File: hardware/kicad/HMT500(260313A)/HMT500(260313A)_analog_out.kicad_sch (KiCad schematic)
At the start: 27 parts, among them U10 TPS26611, U12 OPA197IDBVR, U13 OPA197IDBVR, U7 DAC8760IPWP, U8 DAC8760IPWP, U9 TPS26611

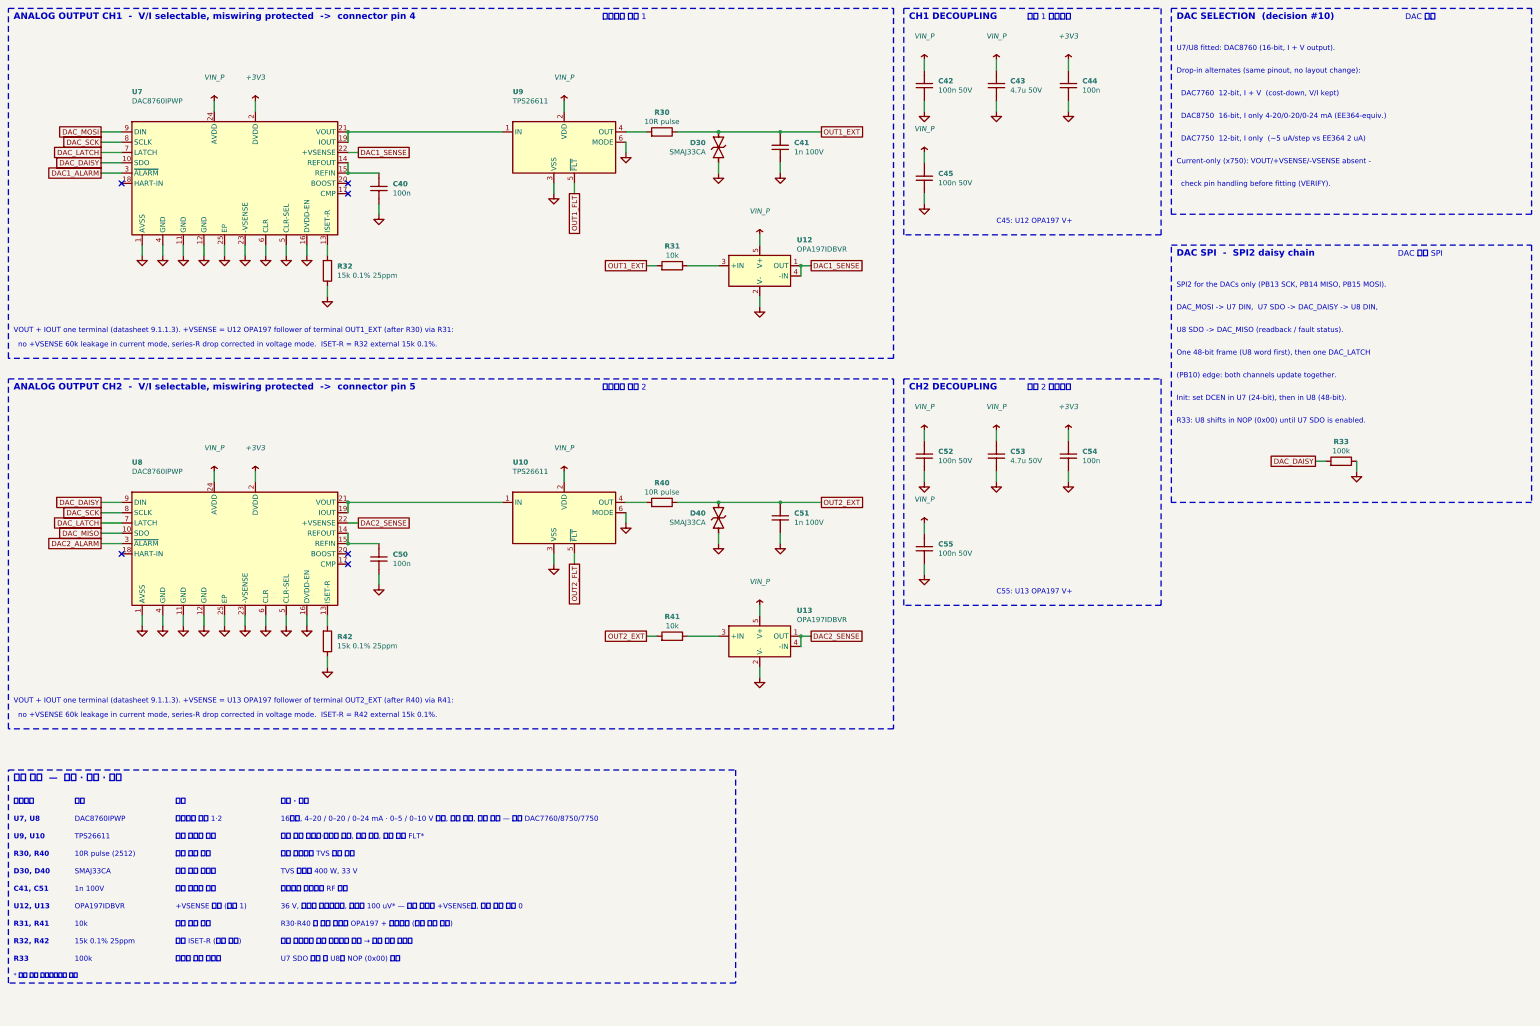
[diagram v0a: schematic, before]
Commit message: Schematic v0.8: apply datasheet review A-O (HMT500(260313A))
- Real pinouts from manufacturer datasheets: LMR36006BRNXR (RNX-12),
  TPS26611DDFR (SOT-23-8), PCAP04 (QFN24); TPS2660 PowerPAD = RTN
- TPS2660: RTN isolated from GND (R22, R7 removed); R5/R6/C4/MODE on
  EF_RTN; R6 80.6k (149 mA); R5 41.2k -> OVP 29 V, supply 12-28 V so
  TPS26611 +Vs stays <= 30 V
- DAC SPI: per-DAC SCLK gating (74LVC2G32, SPI2 mode 3, LATCH1/2 on
  PB10/PB11) - daisy chain was removed in DAC8760 rev D
- DAC AVDD 10R series, ALARM wired-OR with 10k pull-up (PB6)
- Output TVS -> TVS3301 (stacked-pin two-terminal symbol)
- PCAP04 on dedicated SPI3 (PB3/4/5), VDD18 4.7uF, VDD33 10uF
- Buck per datasheet: L 15uH, COUT 2x22uF, CFF 20pF
- Shared VIN_P bulk (C53, C26 removed); PWR_FLT PB7; SGOOD -> PC6/PC7
- Parts list, circuit-design, decision log #26, review doc updated;
  netlist 74/74, 0 errors; tests pass

Co-Authored-By: Claude Opus 5.5 <noreply@anthropic.com>
Claude-Session: https://claude.ai/code/session_01JA2o8uJsqp9Vzsg4b665ev
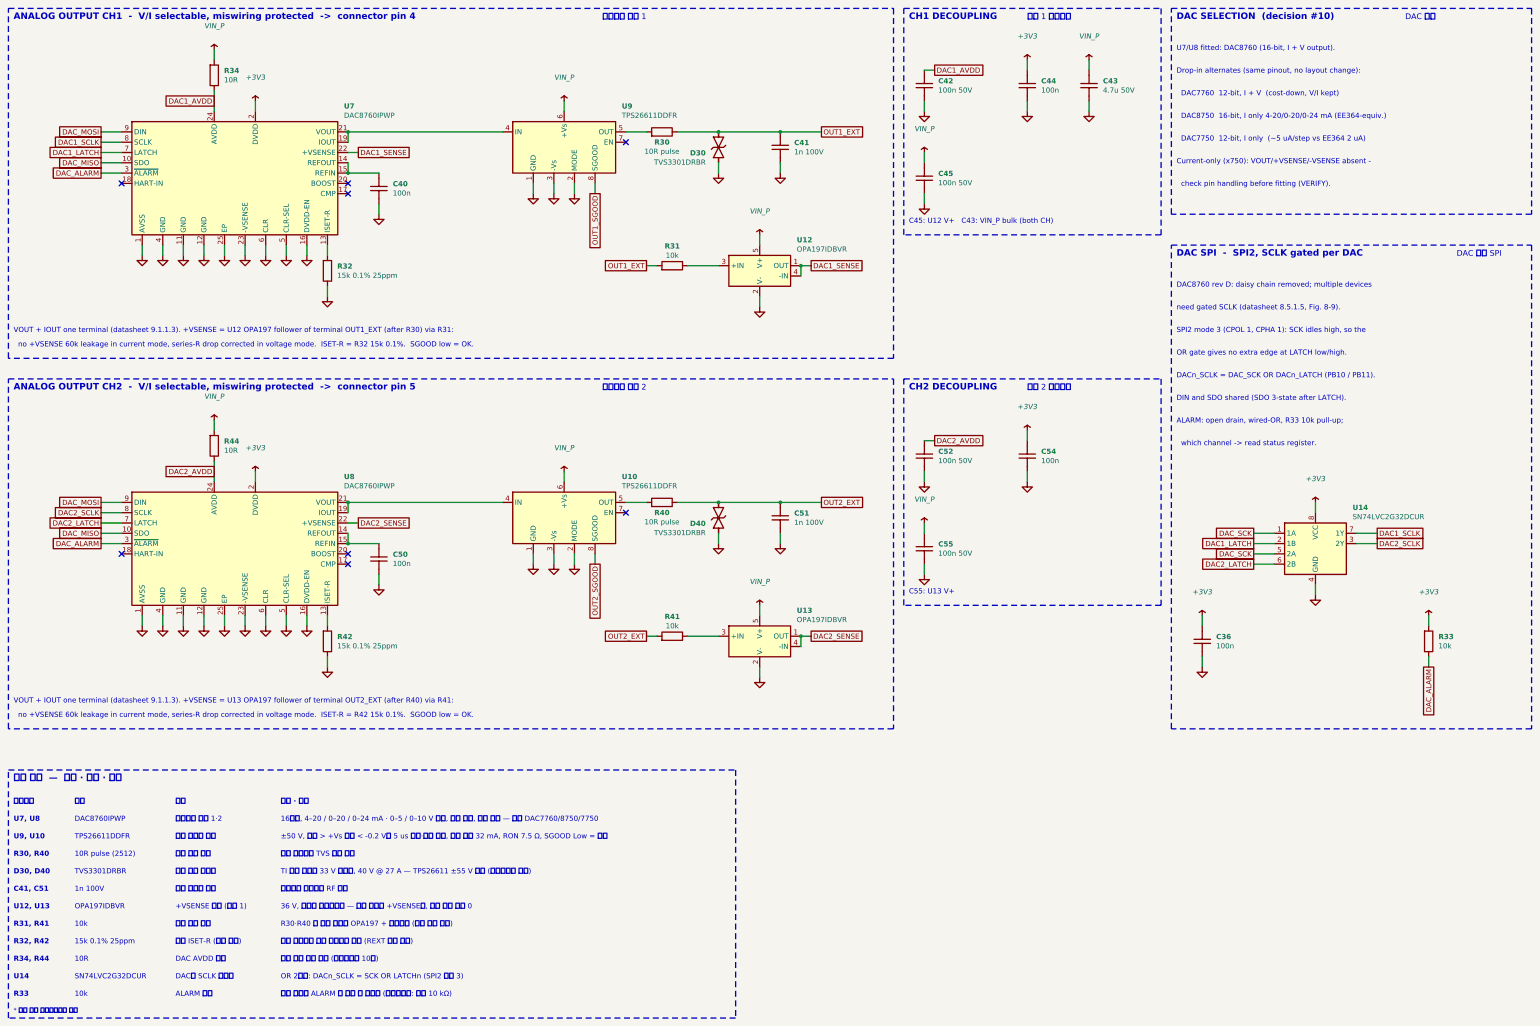
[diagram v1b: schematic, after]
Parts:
- removed C53: 4.7u 50V, Capacitor_SMD:C_1210_3225Metric, symbol HMT500_260313A:C
- added C36: 100n, Capacitor_SMD:C_0603_1608Metric, symbol HMT500_260313A:C
- added R34, R44: 10R, Resistor_SMD:R_0603_1608Metric, symbol HMT500_260313A:R
- added U14: SN74LVC2G32DCUR, Package_SO:VSSOP-8_2.3x2mm_P0.5mm, symbol HMT500_260313A:74LVC2G32
- D30, D40: value SMAJ33CA -> TVS3301DRBR; footprint Diode_SMD:D_SMA -> Package_DFN_QFN:Texas_DRB0008A; symbol HMT500_260313A:TVS_BI -> HMT500_260313A:TVS3301
- R33: value 100k -> 10k
- U10, U9: value TPS26611 -> TPS26611DDFR; footprint TBD:TPS26611 -> Package_TO_SOT_SMD:Texas_DDF0008A_SOT-8_1.6x2.9mm_P0.65mm; VERIFY YES - pin numbers are placeholders -> (none)
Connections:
- net DAC2_ALARM is gone; now on net DAC_ALARM: U8.3 (~{ALARM})
- net OUT1_FLT is gone; now on an unnamed net: U9.5 (OUT)
- net OUT2_FLT is gone; now on an unnamed net: U10.5 (OUT)
- net +3V3: now also R33.1, C36.1, U14.8 (VCC)
- net DAC_MISO: now also U7.10 (SDO)
- net DAC_MOSI: now also U8.9 (DIN)
- net DAC_SCK: now also U14.1 (1A), U14.5 (2A); no longer U7.8 (SCLK), U8.8 (SCLK)
- net GND: now also D30.5, D30.6, D30.7, D30.8, D40.5, D40.6, D40.7, D40.8, U10.1 (GND), U10.2 (MODE), U9.1 (GND), U9.2 (MODE), C36.2, U14.4 (GND); no longer D30.2, D40.2, R33.2, U10.6 (MODE), U9.6 (MODE)
- net OUT1_EXT: now also D30.2, D30.3, D30.4
- net OUT2_EXT: now also D40.2, D40.3, D40.4
- net VIN_P: now also U10.6 (+Vs), U9.6 (+Vs), R34.1, R44.1; no longer C42.1, C52.1, U10.2 (VDD), U7.24 (AVDD), U8.24 (AVDD), U9.2 (VDD)
- net at R30.1: no longer U9.4 (OUT)
- net at U8.19 (IOUT), U8.21 (VOUT): now also U10.4 (IN); no longer U10.1 (IN)
- net at R40.1: no longer U10.4 (OUT)
- net at U7.19 (IOUT), U7.21 (VOUT): now also U9.4 (IN); no longer U9.1 (IN)
- net DAC1_ALARM renamed DAC_ALARM
- net DAC_ALARM: now also R33.2
- removed net DAC_DAISY: R33.1, U7.10 (SDO), U8.9 (DIN)
- net DAC_LATCH renamed DAC1_LATCH
- net DAC1_LATCH: now also U14.2 (1B); no longer U8.7 (LATCH)
- new net DAC1_AVDD: C42.1, R34.2, U7.24 (AVDD)
- new net DAC1_SCLK: U14.7 (1Y), U7.8 (SCLK)
- new net DAC2_AVDD: C52.1, R44.2, U8.24 (AVDD)
- new net DAC2_LATCH: U14.6 (2B), U8.7 (LATCH)
- new net DAC2_SCLK: U14.3 (2Y), U8.8 (SCLK)
- new net OUT1_SGOOD: U9.8 (SGOOD)
- new net OUT2_SGOOD: U10.8 (SGOOD)
- no-connect marks 6 -> 8
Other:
- note added: "10R"
- note added: "36 V, 입출력 레일투레일 — 단자 전압을 +VSENSE로, 전류 모드 누설 0"
- note added: "ALARM 풀업"
- note added: "ALARM: open drain, wired-OR, R33 10k pull-up;"
- note added: "C45: U12 V+ C43: VIN_P bulk (both CH)"
- note added: "C55: U13 V+"
- note added: "DAC AVDD 직렬"
- note added: "DAC SPI - SPI2, SCLK gated per DAC"
- note added: "DAC8760 rev D: daisy chain removed; multiple devices"
- note added: "DACn_SCLK = DAC_SCK OR DACn_LATCH (PB10 / PB11)."
- note added: "DAC별 SCLK 게이트"
- note added: "DIN and SDO shared (SDO 3-state after LATCH)."
- note added: "OR 2회로: DACn_SCLK = SCK OR LATCHn (SPI2 모드 3)"
- note added: "OR gate gives no extra edge at LATCH low/high."
- note added: "R34, R44"
- note added: "SN74LVC2G32DCUR"
- note added: "SPI2 mode 3 (CPOL 1, CPHA 1): SCK idles high, so the"
- note added: "TI 평탄 클램프 33 V 양방향, 40 V @ 27 A — TPS26611 ±55 V 보호 (데이터시트 권장)"
- note added: "TPS26611DDFR"
- note added: "TVS3301DRBR"
- note added: "U14"
- note added: "need gated SCLK (datasheet 8.5.1.5, Fig. 8-9)."
- note added: "no +VSENSE 60k leakage in current mode, series-R drop corrected in voltage mode. ISET-R = R32 15k 0.1%. SGOOD low = OK."
- note added: "no +VSENSE 60k leakage in current mode, series-R drop corrected in voltage mode. ISET-R = R42 15k 0.1%. SGOOD low = OK."
- note added: "which channel -> read status register."
- note added: "±50 V, 단자 > +Vs 또는 < -0.2 V면 5 us 차단·자동 복귀, 전류 제한 32 mA, RON 7.5 Ω, SGOOD Low = 정상"
- note added: "내부 저항보다 온도 드리프트 작음 (REXT 비트 설정)"
- note added: "오픈 드레인 ALARM 두 개를 한 선으로 (데이터시트: 외부 10 kΩ)"
- note added: "전원 상승 속도 제한 (데이터시트 10장)"
- note removed: "(PB10) edge: both channels update together."
- note removed: "100k"
- note removed: "36 V, 입출력 레일투레일, 오프셋 100 uV* — 단자 전압을 +VSENSE로, 전류 모드 누설 0"
- note removed: "C45: U12 OPA197 V+"
- note removed: "C55: U13 OPA197 V+"
- note removed: "DAC SPI - SPI2 daisy chain"
- note removed: "DAC_MOSI -> U7 DIN, U7 SDO -> DAC_DAISY -> U8 DIN,"
- note removed: "Init: set DCEN in U7 (24-bit), then in U8 (48-bit)."
- note removed: "One 48-bit frame (U8 word first), then one DAC_LATCH"
- note removed: "R33: U8 shifts in NOP (0x00) until U7 SDO is enabled."
- note removed: "SMAJ33CA"
- note removed: "SPI2 for the DACs only (PB13 SCK, PB14 MISO, PB15 MOSI)."
- note removed: "TPS26611"
- note removed: "TVS 양방향 400 W, 33 V"
- note removed: "U7 SDO 켜기 전 U8에 NOP (0x00) 입력"
- note removed: "U8 SDO -> DAC_MISO (readback / fault status)."
- note removed: "no +VSENSE 60k leakage in current mode, series-R drop corrected in voltage mode. ISET-R = R32 external 15k 0.1%."
- note removed: "no +VSENSE 60k leakage in current mode, series-R drop corrected in voltage mode. ISET-R = R42 external 15k 0.1%."
- note removed: "내부 저항보다 온도 드리프트 작음 → 전류 출력 정확도"
- note removed: "데이지 체인 풀다운"
- note removed: "출력 단자 과전압·역전압 차단, 전류 제한, 고장 출력 FLT*"
- moved on the sheet: C43, C44, C54, R33

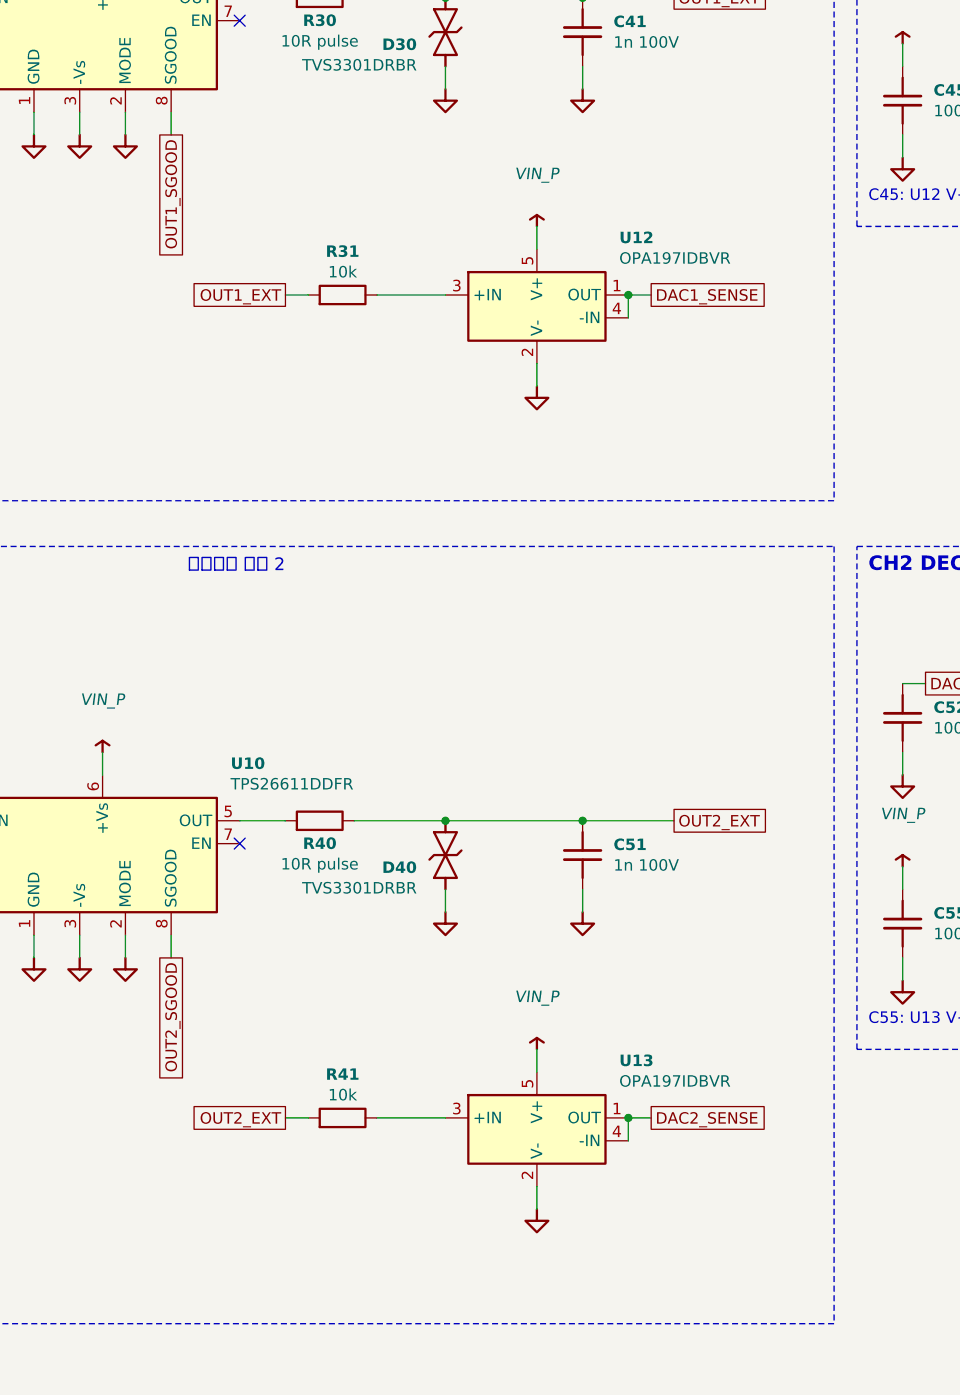
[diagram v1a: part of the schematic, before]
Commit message: Schematic: mirror OPA197 +VSENSE buffers (terminal on right, +VSENSE on left)
Co-Authored-By: Claude Opus 5.5 <noreply@anthropic.com>
Claude-Session: https://claude.ai/code/session_01JA2o8uJsqp9Vzsg4b665ev
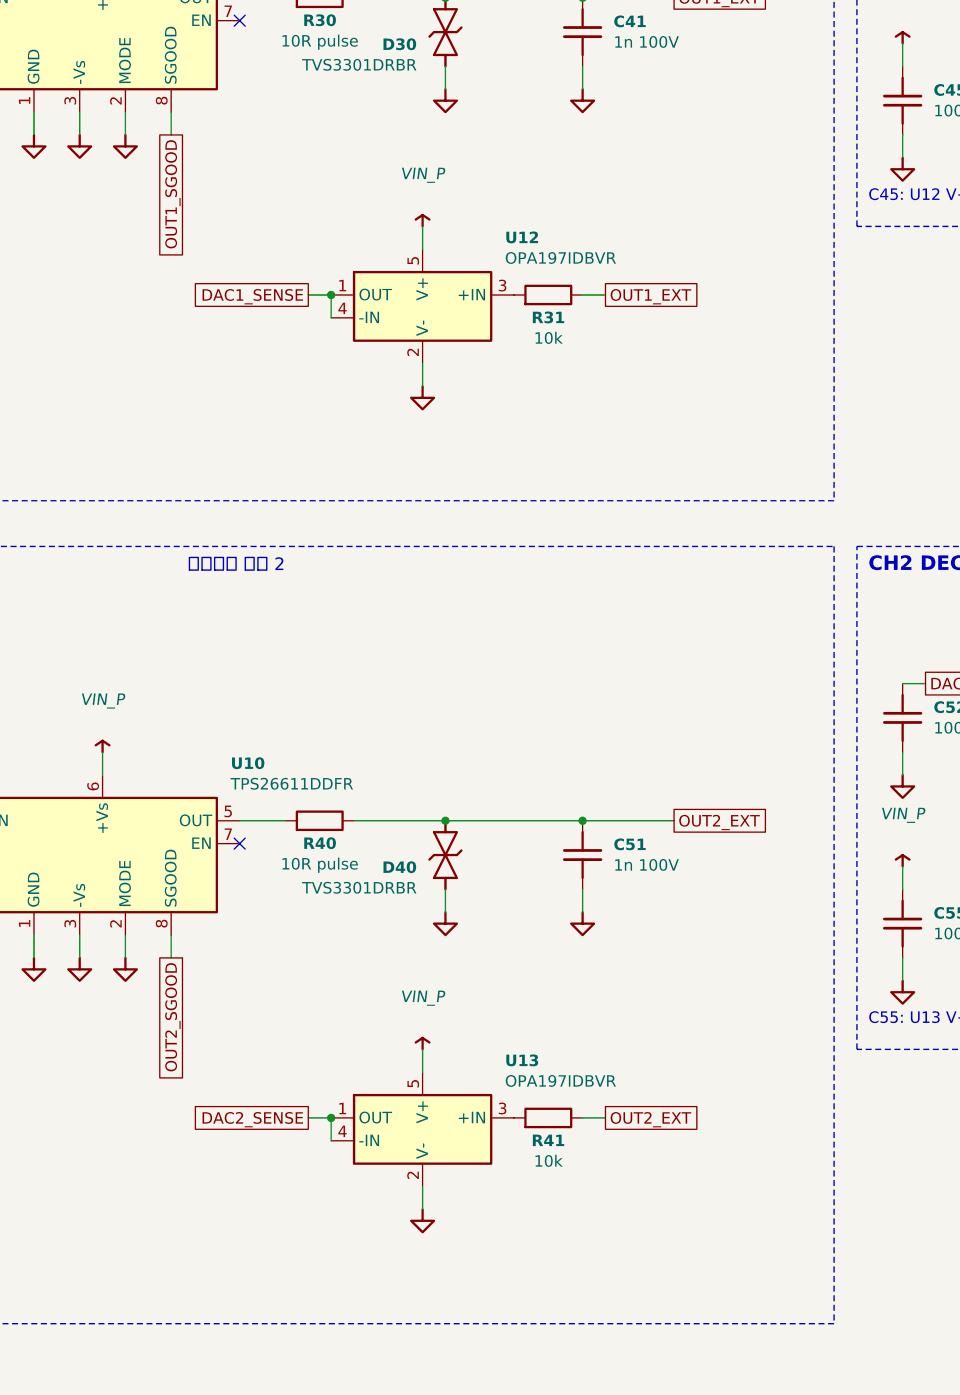
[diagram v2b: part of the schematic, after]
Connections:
- net OUT1_EXT: now also R31.2; no longer R31.1
- net OUT2_EXT: now also R41.2; no longer R41.1
- net at U13.3 (+IN): now also R41.1; no longer R41.2
- net at U12.3 (+IN): now also R31.1; no longer R31.2
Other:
- moved on the sheet: R31, R41, U12, U13

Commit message: Schematic: wire nearby same-sheet nets, signal-flow direction for analog nets
- Analog: +VSENSE and terminal feedback drawn as wires to the OPA197
  buffer (no DACn_SENSE / second OUTn_EXT labels); U14 1A/2A tied, one
  DAC_SCK label
- Power: TPS2660 left pins reordered so R3-R5 run straight from IN to
  UVLO/OVP; one VIN_F label
- Measurement: C27 sits directly between R17/R18 and AIN1/AIN2
- MCU: SWD pads (J2) placed on the PA13/PA14 rows and wired directly
- Label direction for passive nets from signal flow: OUTn_EXT analog ->
  connector, VIN_F connector -> eFuse, BUCK_FB divider -> FB
- Tests: nearby same-sheet labels must be wired; bend limit 6/sheet;
  check_netlist accepts KiCad auto-named multi-pin nets

Co-Authored-By: Claude Opus 5.5 <noreply@anthropic.com>
Claude-Session: https://claude.ai/code/session_01JA2o8uJsqp9Vzsg4b665ev
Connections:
- net DAC1_SENSE: no longer names the net of U12.1 (OUT), U12.4 (-IN), U7.22 (+VSENSE)
- net DAC2_SENSE: no longer names the net of U13.1 (OUT), U13.4 (-IN), U8.22 (+VSENSE)

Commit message: Footprints and part numbers: no TBD left in the schematic
- Project footprint library hardware/kicad/lib/HMT500_260313A.pretty:
  KiCad 7.0.11 footprints + gen_footprints.py (LMR36006 RNX0012A from TI
  land pattern, Bourns 2035-xx-SM GDT, TVS3301 DRB with floating pad)
- GDT changed to 2-electrode Bourns 2035-23-SM-RPLF (2038 is 3-electrode)
- L1 Wurth WE-SL2 744222 (1 mH, 0.8 A); CMC pins renumbered to WE-SL2
  windings 1-4 / 2-3
- J5 Harwin S1941-46R, L2 Coilcraft XGL4030-153MEC, TPS26611 SOT-23-8,
  TPS2660 HTSSOP-16 footprint from 7.0.11
- R1 MMB02070C4708FB200, R30/R40 CRCW251210R0FKEGHP confirmed;
  R19 -> Vishay PLTT0603 0.02 % 5 ppm
- fp-lib-table written by the generator; netlist 74/74, tests pass

Co-Authored-By: Claude Opus 5.5 <noreply@anthropic.com>
Claude-Session: https://claude.ai/code/session_01JA2o8uJsqp9Vzsg4b665ev
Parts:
- D30, D40: footprint Package_DFN_QFN:Texas_DRB0008A -> HMT500_260313A:Texas_DRB0008A_PadFloat
- U10, U9: footprint Package_TO_SOT_SMD:Texas_DDF0008A_SOT-8_1.6x2.9mm_P0.65mm -> Package_TO_SOT_SMD:SOT-23-8

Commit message: Schematic v0.9 + placement rev 4: apply triple-review A/B items, re-review fixes
- Power: OVP 32.6 V (R5 36.5k), D2 TVS3301, C2 2.2u 100V, buck input 220n x2,
  U2 pin 3 = SW; TPS26611 +Vs emitter-follower clamp (Q1 MMBTA06, R50, D50 27V)
- RS-485: THVD2410, DE 10k pull-down (R60) for in-house bootloader
- MCU: SGOOD on PA0/PA4, CS_CDC PA15, VIN_SENSE PB0, LATCH/CS pull-ups,
  SWD no-connect removed, netlist checker flags no-connect on used pins
- Analog: OPA197 V+ = DAC AVDD, R31/R41 100k, local caps; X7R throughout
- New aux sheet; SOT-23 and R1206 footprints; parts list and JLC files
- Placement: pin-targeted hints, MCU decaps under U4, chassis parts grouped
  in front, J5 keep-out 3.3 mm, CHASSIS netclass; 102/102 parts placed
- Docs: final review H table, decision #32, circuit design, placement rev 4

Co-Authored-By: Claude Opus 5.5 <noreply@anthropic.com>
Claude-Session: https://claude.ai/code/session_01JA2o8uJsqp9Vzsg4b665ev
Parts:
- R31, R41: value 10k -> 100k
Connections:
- net DAC1_AVDD: now also C45.1, U12.5 (V+)
- net DAC2_AVDD: now also C55.1, U13.5 (V+)
- net VIN_P: no longer C45.1, C55.1, U10.6 (+Vs), U12.5 (V+), U13.5 (V+), U9.6 (+Vs)
- new net VS_CLAMP: U10.6 (+Vs), U9.6 (+Vs)
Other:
- note added: "100k"
- note added: "36 V, 입출력 레일투레일 — 단자 전압을 +VSENSE로, 전류 모드 누설 0. V+ = DAC AVDD"
- note added: "C45: U12 V+ (AVDD) C43: VIN_P bulk"
- note added: "C55: U13 V+ (AVDD)"
- note added: "R30·R40 뒤 단자 전압을 OPA197 + 입력으로 (서지 전류 제한, ±30 V 오배선 9 mW, v0.9)"
- note added: "±50 V, 단자 > +Vs 또는 < -0.2 V면 5 us 차단·자동 복귀, 전류 제한 32 mA, RON 7.5 Ω, SGOOD Low = 정상. +Vs = VS_CLAMP (27 V 제너, 시트 Aux)"
- note removed: "36 V, 입출력 레일투레일 — 단자 전압을 +VSENSE로, 전류 모드 누설 0"
- note removed: "C45: U12 V+ C43: VIN_P bulk (both CH)"
- note removed: "C55: U13 V+"
- note removed: "R30·R40 뒤 단자 전압을 OPA197 + 입력으로 (서지 전류 제한)"
- note removed: "±50 V, 단자 > +Vs 또는 < -0.2 V면 5 us 차단·자동 복귀, 전류 제한 32 mA, RON 7.5 Ω, SGOOD Low = 정상"
- moved on the sheet: C40, C45, C50, C55
